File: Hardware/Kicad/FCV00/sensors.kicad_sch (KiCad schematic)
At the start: 14 parts, among them U6 ICM-42688-P, U7 LPS22DF, U8 W25Q128JVSIQ

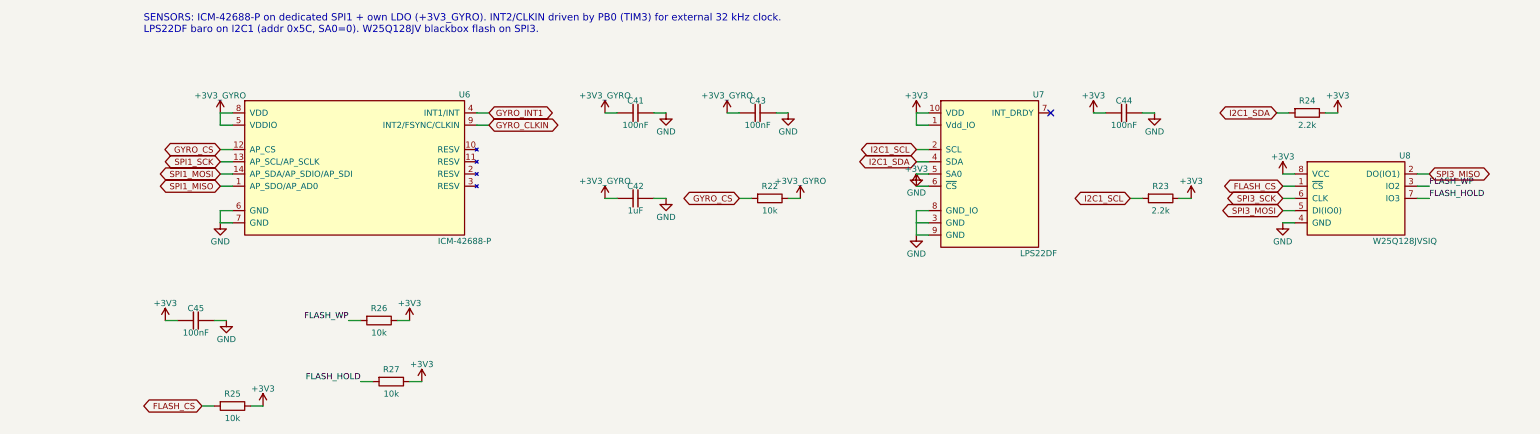
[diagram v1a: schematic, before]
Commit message: Boards follow the B0_EE part convention
- every real part uses the symbol/footprint/3D/datasheet named after its MPN in Kicad_Libs
- symbols keep only Reference, Value, Footprint, Datasheet, Description
  (MPN, Manufacturer, Verify, LCSC, Note fields removed; Verify notes moved to the Readme)
- schematic symbol caches rebuilt from the libraries, PCB footprints relinked with the
  same fields and 3D models as the library (connectivity unchanged)
- DNP and BOM attributes of the footprints match the symbols
- BOMs re-exported with kicad-cli
- ignore KiCad local history
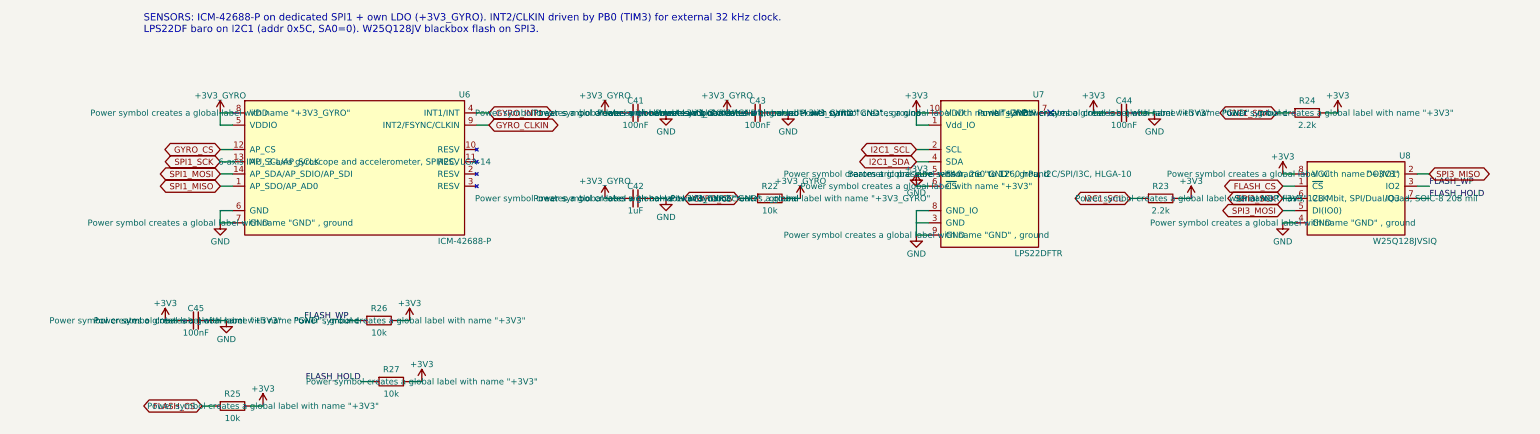
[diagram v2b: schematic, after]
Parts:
- U6: footprint eSensor:Bosch_LGA-14_3x2.5mm_P0.5mm -> eSensor:ICM-42688-P; MPN ICM-42688-P -> (none); Manufacturer TDK InvenSense -> (none); Verify Pin table from KiCad IIM-42652 (same LGA-14 package/pinout 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 -> (none)
- U7: value LPS22DF -> LPS22DFTR; footprint eSensor:ST_HLGA-10_2x2mm_P0.5mm_LayoutBorder3x2y -> eSensor:LPS22DFTR; symbol eSensor:LPS22DF -> eSensor:LPS22DFTR; MPN LPS22DFTR -> (none); Manufacturer STMicroelectronics -> (none)
- U8: footprint eMemory:SOIC-8_5.23x5.23mm_P1.27mm -> eMemory:W25Q128JVSIQ; LCSC C97521 -> (none); MPN W25Q128JVSIQ -> (none); Manufacturer Winbond -> (none)
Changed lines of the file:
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@@
 			)
 		)
-		(property "Description" ""
+		(property "Description" "Power symbol creates a global label with name \"+3V3_GYRO\""
 			(at 107.95 35.56 0)
 			(show_name no)
@@
 	)
 	(symbol
-		(lib_id "eSensor:LPS22DF")
+		(lib_id "eSensor:LPS22DFTR")
 		(at 187.96 48.26 0)
 		(unit 1)
@@
 			)
 		)
-		(property "Value" "LPS22DF"
+		(property "Value" "LPS22DFTR"
 			(at 198.12 64.77 0)
 			(show_name no)
@@
 			)
 		)
-		(property "Footprint" "eSensor:ST_HLGA-10_2x2mm_P0.5mm_LayoutBorder3x2y"
+		(property "Footprint" "eSensor:LPS22DFTR"
 			(at 187.96 48.26 0)
 			(hide yes)
@@
 			)
 		)
-		(property "Datasheet" "https://www.st.com/resource/en/datasheet/lps22df.pdf"
+		(property "Datasheet" "${KIPRJMOD}/../KiCad_Libs/eSensor/datasheet/LPS22DFTR.pdf"
 			(at 187.96 48.26 0)
 			(hide yes)
@@
 			)
 		)
-		(property "Description" ""
+		(property "Description" "Barometric pressure sensor, 260 to 1260 hPa, I2C/SPI/I3C, HLGA-10"
 			(at 187.96 48.26 0)
-			(show_name no)
-			(do_not_autoplace no)
-			(effects
-				(font
-					(size 1.27 1.27)
-				)
-			)
-		)
-		(property "Manufacturer" "STMicroelectronics"
-			(at 187.96 48.26 0)
-			(hide yes)
-			(show_name no)
-			(do_not_autoplace no)
-			(effects
-				(font
-					(size 1.27 1.27)
-				)
-			)
-		)
-		(property "MPN" "LPS22DFTR"
-			(at 187.96 48.26 0)
-			(hide yes)
 			(show_name no)
 			(do_not_autoplace no)
@@
 			)
 		)
-		(property "Description" ""
+		(property "Description" "Power symbol creates a global label with name \"GND\" , ground"
 			(at 172.72 48.26 0)
 			(show_name no)
@@
 			)
 		)
-		(property "Description" ""
+		(property "Description" "Power symbol creates a global label with name \"+3V3_GYRO\""
 			(at 107.95 53.34 0)
 			(show_name no)
@@
 			)
 		)
-		(property "Description" ""
+		(property "Description" "Power symbol creates a global label with name \"+3V3\""
 			(at 172.72 35.56 0)
 			(show_name no)
@@
 			)
 		)
-		(property "Description" ""
+		(property "Description" "Power symbol creates a global label with name \"+3V3\""
 			(at 172.72 50.8 0)
 			(show_name no)
@@
 			)
 		)
-		(property "Description" ""
+		(property "Description" "Power symbol creates a global label with name \"+3V3\""
 			(at 260.35 35.56 0)
 			(show_name no)
@@
 			)
 		)
-		(property "Description" ""
+		(property "Description" "Power symbol creates a global label with name \"+3V3\""
 			(at 69.85 91.44 0)
 			(show_name no)
@@
 			)
 		)
-		(property "Description" ""
+		(property "Description" "Power symbol creates a global label with name \"GND\" , ground"
 			(at 222.25 35.56 0)
 			(show_name no)
@@
 			)
 		)
-		(property "Description" ""
+		(property "Description" "Power symbol creates a global label with name \"+3V3\""
 			(at 248.92 48.26 0)
 			(show_name no)
@@
 			)
 		)
-		(property "Footprint" "eSensor:Bosch_LGA-14_3x2.5mm_P0.5mm"
+		(property "Footprint" "eSensor:ICM-42688-P"
 			(at 55.88 45.72 0)
 			(hide yes)
@@
 			)
 		)
-		(property "Datasheet" "https://invensense.tdk.com/wp-content/uploads/2020/04/ds-000347_icm-42688-p-datasheet.pdf"
+		(property "Datasheet" "${KIPRJMOD}/../KiCad_Libs/eSensor/datasheet/ICM-42688-P.pdf"
 			(at 55.88 45.72 0)
 			(hide yes)
@@
 			)
 		)
-		(property "Description" ""
+		(property "Description" "6-axis IMU, 3-axis gyroscope and accelerometer, SPI/I2C, LGA-14"
 			(at 55.88 45.72 0)
-			(show_name no)
-			(do_not_autoplace no)
-			(effects
-				(font
-					(size 1.27 1.27)
-				)
-			)
-		)
-		(property "Manufacturer" "TDK InvenSense"
-			(at 55.88 45.72 0)
-			(hide yes)
-			(show_name no)
-			(do_not_autoplace no)
-			(effects
-				(font
-					(size 1.27 1.27)
-				)
-			)
-		)
-		(property "MPN" "ICM-42688-P"
-			(at 55.88 45.72 0)
-			(hide yes)
-			(show_name no)
-			(do_not_autoplace no)
-			(effects
-				(font
-					(size 1.27 1.27)
-				)
-			)
-		)
-		(property "Verify" "Pin table from KiCad IIM-42652 (same LGA-14 package/pinout as ICM-42688-P). Confirm pin 7/RESV handling vs DS-000347."
-			(at 55.88 45.72 0)
-			(hide yes)
 			(show_name no)
 			(do_not_autoplace no)
@@
 			)
 		)
-		(property "Description" ""
+		(property "Description" "Power symbol creates a global label with name \"GND\" , ground"
 			(at 120.65 53.34 0)
 			(show_name no)
@@
 			)
 		)
-		(property "Description" ""
+		(property "Description" "Power symbol creates a global label with name \"+3V3\""
 			(at 229.87 53.34 0)
 			(show_name no)
@@
 			)
 		)
-		(property "Description" ""
+		(property "Description" "Power symbol creates a global label with name \"GND\" , ground"
 			(at 29.21 78.74 0)
 			(show_name no)
@@
 			)
 		)
-		(property "Description" ""
+		(property "Description" "Power symbol creates a global label with name \"GND\" , ground"
 			(at 120.65 35.56 0)
 			(show_name no)
@@
 			)
 		)
-		(property "Footprint" "eMemory:SOIC-8_5.23x5.23mm_P1.27mm"
+		(property "Footprint" "eMemory:W25Q128JVSIQ"
 			(at 264.16 53.34 0)
 			(hide yes)
@@
 			)
 		)
-		(property "Datasheet" "https://www.winbond.com/hq/product/code-storage-flash-memory/serial-nor-flash/?__locale=en&partNo=W25Q128JV"
+		(property "Datasheet" "${KIPRJMOD}/../KiCad_Libs/eMemory/datasheet/W25Q128JVSIQ.pdf"
 			(at 264.16 53.34 0)
 			(hide yes)
@@
 			)
 		)
-		(property "Description" ""
+		(property "Description" "Serial NOR flash, 128 Mbit, SPI/Dual/Quad, SOIC-8 208 mil"
 			(at 264.16 53.34 0)
-			(show_name no)
-			(do_not_autoplace no)
-			(effects
-				(font
-					(size 1.27 1.27)
-				)
-			)
-		)
-		(property "Manufacturer" "Winbond"
-			(at 264.16 53.34 0)
-			(hide yes)
-			(show_name no)
-			(do_not_autoplace no)
-			(effects
-				(font
-					(size 1.27 1.27)
-				)
-			)
-		)
-		(property "MPN" "W25Q128JVSIQ"
-			(at 264.16 53.34 0)
-			(hide yes)
-			(show_name no)
-			(do_not_autoplace no)
-			(effects
-				(font
-					(size 1.27 1.27)
-				)
-			)
-		)
-		(property "LCSC" "C97521"
-			(at 264.16 53.34 0)
-			(hide yes)
 			(show_name no)
 			(do_not_autoplace no)
@@
 			)
 		)
-		(property "Description" ""
+		(property "Description" "Power symbol creates a global label with name \"+3V3_GYRO\""
 			(at 148.59 53.34 0)
 			(show_name no)
@@
 			)
 		)
-		(property "Description" ""
+		(property "Description" "Power symbol creates a global label with name \"GND\" , ground"
 			(at 27.94 58.42 0)
 			(show_name no)
@@
 			)
 		)
-		(property "Description" ""
+		(property "Description" "Power symbol creates a global label with name \"GND\" , ground"
 			(at 248.92 58.42 0)
 			(show_name no)
@@
 			)
 		)
-		(property "Description" ""
+		(property "Description" "Power symbol creates a global label with name \"+3V3\""
 			(at 16.51 78.74 0)
 			(show_name no)
@@
 			)
 		)
-		(property "Description" ""
+		(property "Description" "Power symbol creates a global label with name \"+3V3_GYRO\""
 			(at 27.94 35.56 0)
 			(show_name no)
@@
 			)
 		)
-		(property "Description" ""
+		(property "Description" "Power symbol creates a global label with name \"GND\" , ground"
 			(at 146.05 35.56 0)
 			(show_name no)
@@
 			)
 		)
-		(property "Description" ""
+		(property "Description" "Power symbol creates a global label with name \"+3V3_GYRO\""
 			(at 133.35 35.56 0)
 			(show_name no)
@@
 			)
 		)
-		(property "Description" ""
+		(property "Description" "Power symbol creates a global label with name \"+3V3\""
 			(at 36.83 96.52 0)
 			(show_name no)
@@
 			)
 		)
-		(property "Description" ""
+		(property "Description" "Power symbol creates a global label with name \"+3V3\""
 			(at 67.31 78.74 0)
 			(show_name no)
@@
 			)
 		)
-		(property "Description" ""
+		(property "Description" "Power symbol creates a global label with name \"+3V3\""
 			(at 209.55 35.56 0)
 			(show_name no)
@@
 			)
 		)
-		(property "Description" ""
+		(property "Description" "Power symbol creates a global label with name \"GND\" , ground"
 			(at 172.72 60.96 0)
 			(show_name no)

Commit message: Cleared all the descriptions and started Power section for FCV
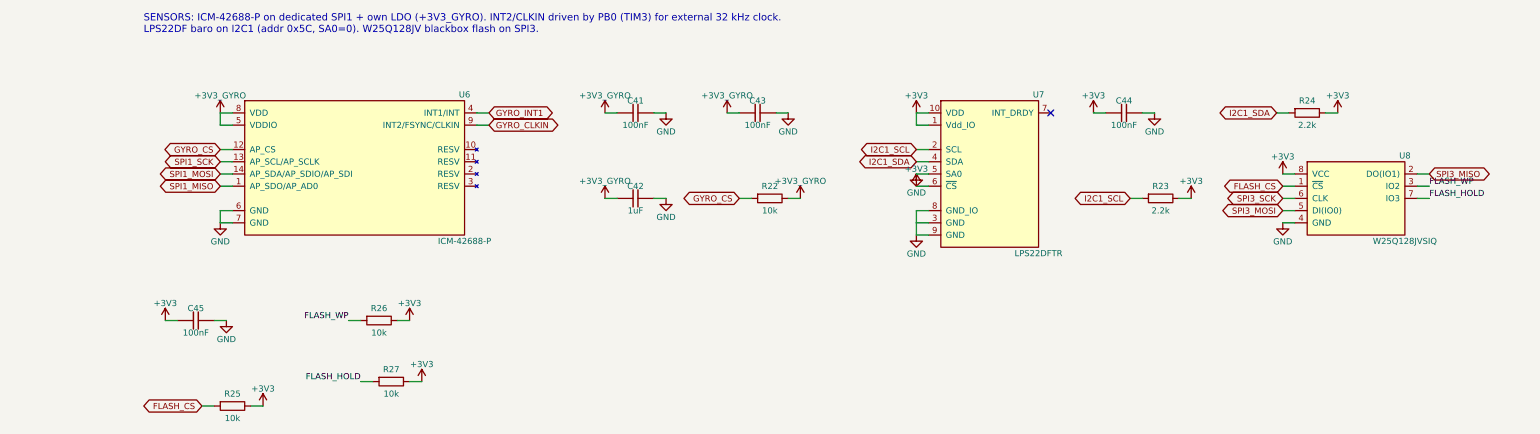
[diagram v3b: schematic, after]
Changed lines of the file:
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@@
 		(property "Description" "Power symbol creates a global label with name \"+3V3_GYRO\""
 			(at 107.95 35.56 0)
+			(hide yes)
 			(show_name no)
 			(do_not_autoplace no)
@@
 		(property "Description" "Barometric pressure sensor, 260 to 1260 hPa, I2C/SPI/I3C, HLGA-10"
 			(at 187.96 48.26 0)
+			(hide yes)
 			(show_name no)
 			(do_not_autoplace no)
@@
 		(property "Description" "Power symbol creates a global label with name \"GND\" , ground"
 			(at 172.72 48.26 0)
+			(hide yes)
 			(show_name no)
 			(do_not_autoplace no)
@@
 		(property "Description" "Power symbol creates a global label with name \"+3V3_GYRO\""
 			(at 107.95 53.34 0)
+			(hide yes)
 			(show_name no)
 			(do_not_autoplace no)
@@
 		(property "Description" "Power symbol creates a global label with name \"+3V3\""
 			(at 172.72 35.56 0)
+			(hide yes)
 			(show_name no)
 			(do_not_autoplace no)
@@
 		(property "Description" "Power symbol creates a global label with name \"+3V3\""
 			(at 172.72 50.8 0)
+			(hide yes)
 			(show_name no)
 			(do_not_autoplace no)
@@
 		(property "Description" "Power symbol creates a global label with name \"+3V3\""
 			(at 260.35 35.56 0)
+			(hide yes)
 			(show_name no)
 			(do_not_autoplace no)
@@
 		(property "Description" "Power symbol creates a global label with name \"+3V3\""
 			(at 69.85 91.44 0)
+			(hide yes)
 			(show_name no)
 			(do_not_autoplace no)
@@
 		(property "Description" "Power symbol creates a global label with name \"GND\" , ground"
 			(at 222.25 35.56 0)
+			(hide yes)
 			(show_name no)
 			(do_not_autoplace no)
@@
 		(property "Description" "Power symbol creates a global label with name \"+3V3\""
 			(at 248.92 48.26 0)
+			(hide yes)
 			(show_name no)
 			(do_not_autoplace no)
@@
 		(property "Description" "6-axis IMU, 3-axis gyroscope and accelerometer, SPI/I2C, LGA-14"
 			(at 55.88 45.72 0)
+			(hide yes)
 			(show_name no)
 			(do_not_autoplace no)
@@
 		(property "Description" "Power symbol creates a global label with name \"GND\" , ground"
 			(at 120.65 53.34 0)
+			(hide yes)
 			(show_name no)
 			(do_not_autoplace no)
@@
 		(property "Description" "Power symbol creates a global label with name \"+3V3\""
 			(at 229.87 53.34 0)
+			(hide yes)
 			(show_name no)
 			(do_not_autoplace no)
@@
 		(property "Description" "Power symbol creates a global label with name \"GND\" , ground"
 			(at 29.21 78.74 0)
+			(hide yes)
 			(show_name no)
 			(do_not_autoplace no)
@@
 		(property "Description" "Power symbol creates a global label with name \"GND\" , ground"
 			(at 120.65 35.56 0)
+			(hide yes)
 			(show_name no)
 			(do_not_autoplace no)
@@
 		(property "Description" "Serial NOR flash, 128 Mbit, SPI/Dual/Quad, SOIC-8 208 mil"
 			(at 264.16 53.34 0)
+			(hide yes)
 			(show_name no)
 			(do_not_autoplace no)
@@
 		(property "Description" "Power symbol creates a global label with name \"+3V3_GYRO\""
 			(at 148.59 53.34 0)
+			(hide yes)
 			(show_name no)
 			(do_not_autoplace no)
@@
 		(property "Description" "Power symbol creates a global label with name \"GND\" , ground"
 			(at 27.94 58.42 0)
+			(hide yes)
 			(show_name no)
 			(do_not_autoplace no)
@@
 		(property "Description" "Power symbol creates a global label with name \"GND\" , ground"
 			(at 248.92 58.42 0)
+			(hide yes)
 			(show_name no)
 			(do_not_autoplace no)
@@
 		(property "Description" "Power symbol creates a global label with name \"+3V3\""
 			(at 16.51 78.74 0)
+			(hide yes)
 			(show_name no)
 			(do_not_autoplace no)
@@
 		(property "Description" "Power symbol creates a global label with name \"+3V3_GYRO\""
 			(at 27.94 35.56 0)
+			(hide yes)
 			(show_name no)
 			(do_not_autoplace no)
@@
 		(property "Description" "Power symbol creates a global label with name \"GND\" , ground"
 			(at 146.05 35.56 0)
+			(hide yes)
 			(show_name no)
 			(do_not_autoplace no)
@@
 		(property "Description" "Power symbol creates a global label with name \"+3V3_GYRO\""
 			(at 133.35 35.56 0)
+			(hide yes)
 			(show_name no)
 			(do_not_autoplace no)
@@
 		(property "Description" "Power symbol creates a global label with name \"+3V3\""
 			(at 36.83 96.52 0)
+			(hide yes)
 			(show_name no)
 			(do_not_autoplace no)
@@
 		(property "Description" "Power symbol creates a global label with name \"+3V3\""
 			(at 67.31 78.74 0)
+			(hide yes)
 			(show_name no)
 			(do_not_autoplace no)
@@
 		(property "Description" "Power symbol creates a global label with name \"+3V3\""
 			(at 209.55 35.56 0)
+			(hide yes)
 			(show_name no)
 			(do_not_autoplace no)
@@
 		(property "Description" "Power symbol creates a global label with name \"GND\" , ground"
 			(at 172.72 60.96 0)
-			(show_name no)
-			(do_not_autoplace no)
+			(hide yes)
+			(show_name no)
+			(do_not_autoplace no)
